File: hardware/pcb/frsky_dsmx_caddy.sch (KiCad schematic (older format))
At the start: 25 parts, among them P1 G9X, P2 Fr-Sky, P3 DSMX, Q1 BC847C, Q2 Si2319DS, Q3 Si2319DS, Q4 BC847C, U1 7805, U2 LN-6206-30

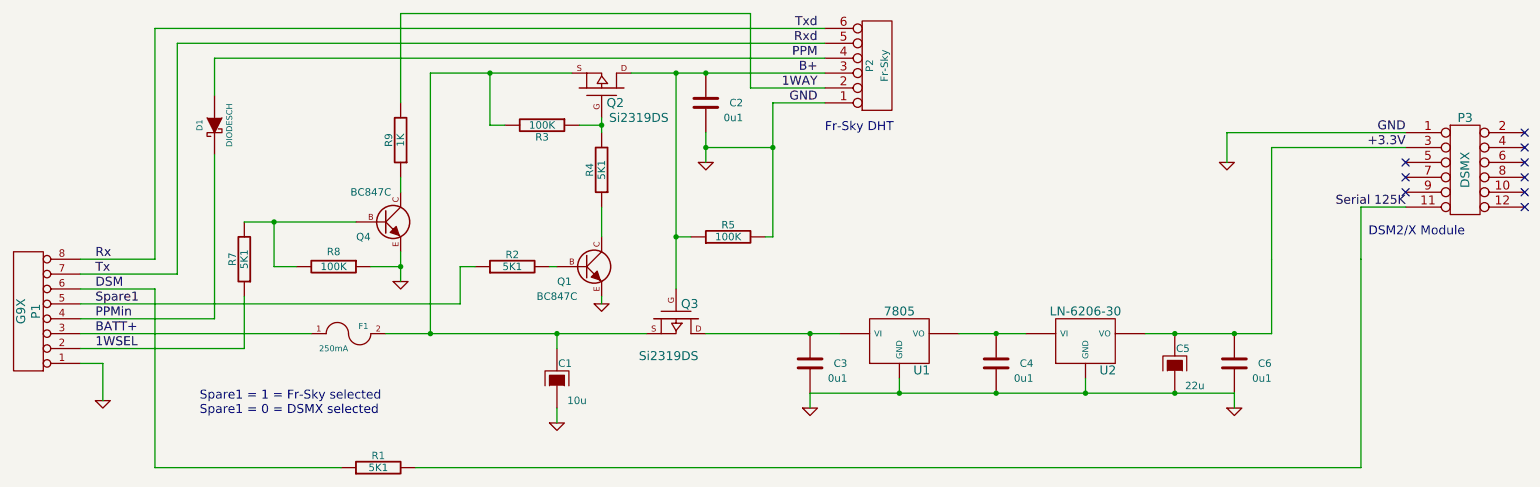
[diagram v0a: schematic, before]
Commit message: Various updates that should have ben committed ages ago, including some updated KiCAD file versions
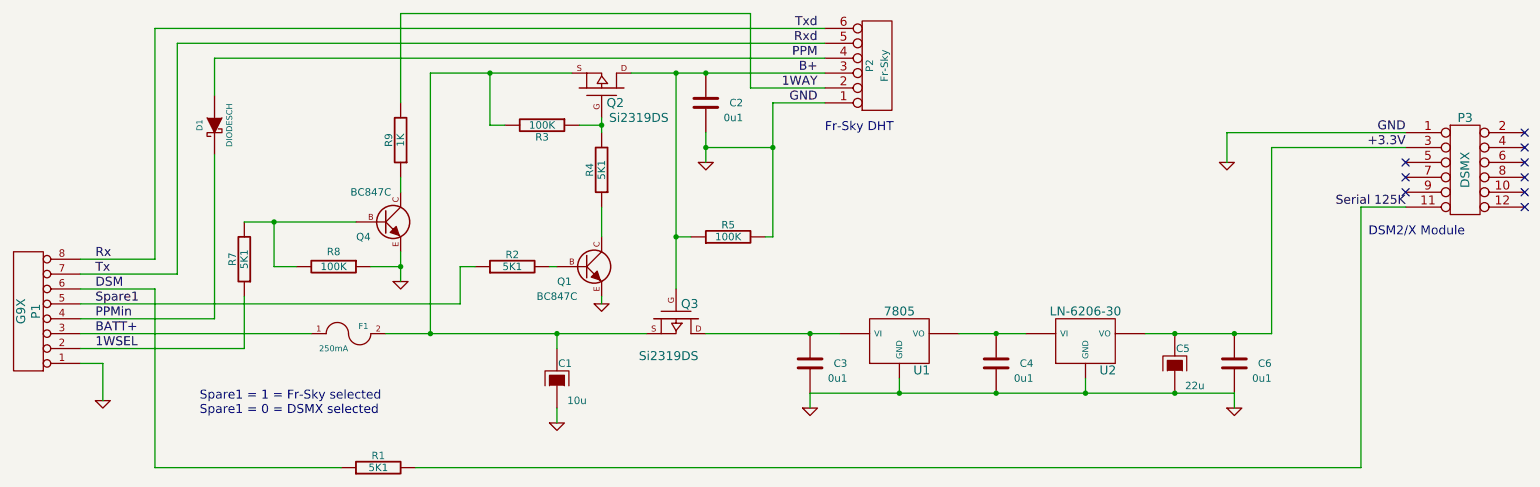
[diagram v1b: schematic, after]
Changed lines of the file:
@@
-EESchema Schematic File Version 2  date Tue 30 Oct 2012 08:21:28 PM NZDT
+EESchema Schematic File Version 2  date Thu 01 Nov 2012 01:36:38 PM NZDT
 LIBS:gruvin
 LIBS:power
@@
 	1750 3200 1750 4400
 Wire Wire Line
-	5250 1750 5250 2850
-Wire Wire Line
-	5250 2850 5250 3200
+	5250 1750 5250 3200
 Connection ~ 5250 2850
 Wire Wire Line
@@
 	2550 3050 2700 3050
 Wire Wire Line
-	3100 2750 2550 2750
-Wire Wire Line
-	2550 2750 2350 2750
+	3100 2750 2350 2750
 Wire Wire Line
 	2350 3250 2350 3600
@@
 	3500 4400 9850 4400
 Wire Wire Line
-	9850 4400 9850 3000
-Wire Wire Line
-	9850 3000 9850 2650
+	9850 4400 9850 2650
 Wire Wire Line
 	9850 2650 10150 2650
@@
 	3800 3300 1250 3300
 Wire Wire Line
-	5450 2150 5450 2250
-Wire Wire Line
-	5450 2250 5450 2350
+	5450 2150 5450 2350
 Connection ~ 5450 2250
 Wire Wire Line
@@
 Connection ~ 9000 3500
 Wire Wire Line
-	9000 3900 8600 3900
-Wire Wire Line
-	8600 3900 8000 3900
-Wire Wire Line
-	8000 3900 7400 3900
-Wire Wire Line
-	7400 3900 6750 3900
-Wire Wire Line
-	6750 3900 6150 3900
+	9000 3900 6150 3900
 Wire Wire Line
 	2150 2300 2150 3400
@@
 Connection ~ 4450 3500
 Wire Wire Line
-	7600 3500 7400 3500
-Wire Wire Line
-	7400 3500 7150 3500
+	7600 3500 7150 3500
 Wire Wire Line
 	4450 3500 4450 3600
 Wire Wire Line
-	8400 3500 8600 3500
-Wire Wire Line
-	8600 3500 9000 3500
-Wire Wire Line
-	9000 3500 9250 3500
-Wire Wire Line
-	4550 1750 4000 1750
-Wire Wire Line
-	4000 1750 3600 1750
-Wire Wire Line
-	4750 2050 4750 2100
-Wire Wire Line
-	4750 2100 4750 2150
+	8400 3500 9250 3500
+Wire Wire Line
+	4550 1750 3600 1750
+Wire Wire Line
+	4750 2050 4750 2150
 Connection ~ 6750 3900
 Connection ~ 6150 3500
 Connection ~ 7400 3900
 Wire Wire Line
-	6250 1750 5450 1750
-Wire Wire Line
-	5450 1750 5250 1750
-Wire Wire Line
-	5250 1750 4950 1750
+	6250 1750 4950 1750
 Wire Wire Line
 	8000 3900 8000 3800
@@
 	1900 3100 1250 3100
 Wire Wire Line
-	9250 3500 9250 3000
-Wire Wire Line
-	9250 3000 9250 2250
+	9250 3500 9250 2250
 Wire Wire Line
 	9250 2250 10150 2250
@@
 	2150 1650 2150 1900
 Wire Wire Line
-	6350 3500 6150 3500
-Wire Wire Line
-	6150 3500 5450 3500
+	6350 3500 5450 3500
 Wire Wire Line
 	1250 3700 1400 3700
@@
 	6250 1950 5900 1950
 Wire Wire Line
-	3400 2950 3400 3050
-Wire Wire Line
-	3400 3050 3400 3150
+	3400 2950 3400 3150
 Wire Wire Line
 	3400 2550 3400 2450
@@
 Connection ~ 3400 3050
 Wire Wire Line
-	3300 3500 3600 3500
-Wire Wire Line
-	3600 3500 4450 3500
-Wire Wire Line
-	4450 3500 5050 3500
+	3300 3500 5050 3500
 Wire Wire Line
 	4450 3050 4400 3050
@@
 	5850 2850 5900 2850
 Wire Wire Line
-	5900 2850 5900 2250
-Wire Wire Line
-	5900 2250 5900 1950
+	5900 2850 5900 1950
 Connection ~ 5900 2250
 $Comp
